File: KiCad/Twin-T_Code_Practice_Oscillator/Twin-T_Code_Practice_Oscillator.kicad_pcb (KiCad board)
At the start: 2 copper layers, 96.5 x 50.8 mm, 52 parts, among them J1 BATT, J2 DC IN, J3 PITCH, J4 VOLUME, J5 KEY, J6 PHONES, J7 SPKR, Q1 PN2222A, Q2 2N7000, U1 TLV272, U2 LM386

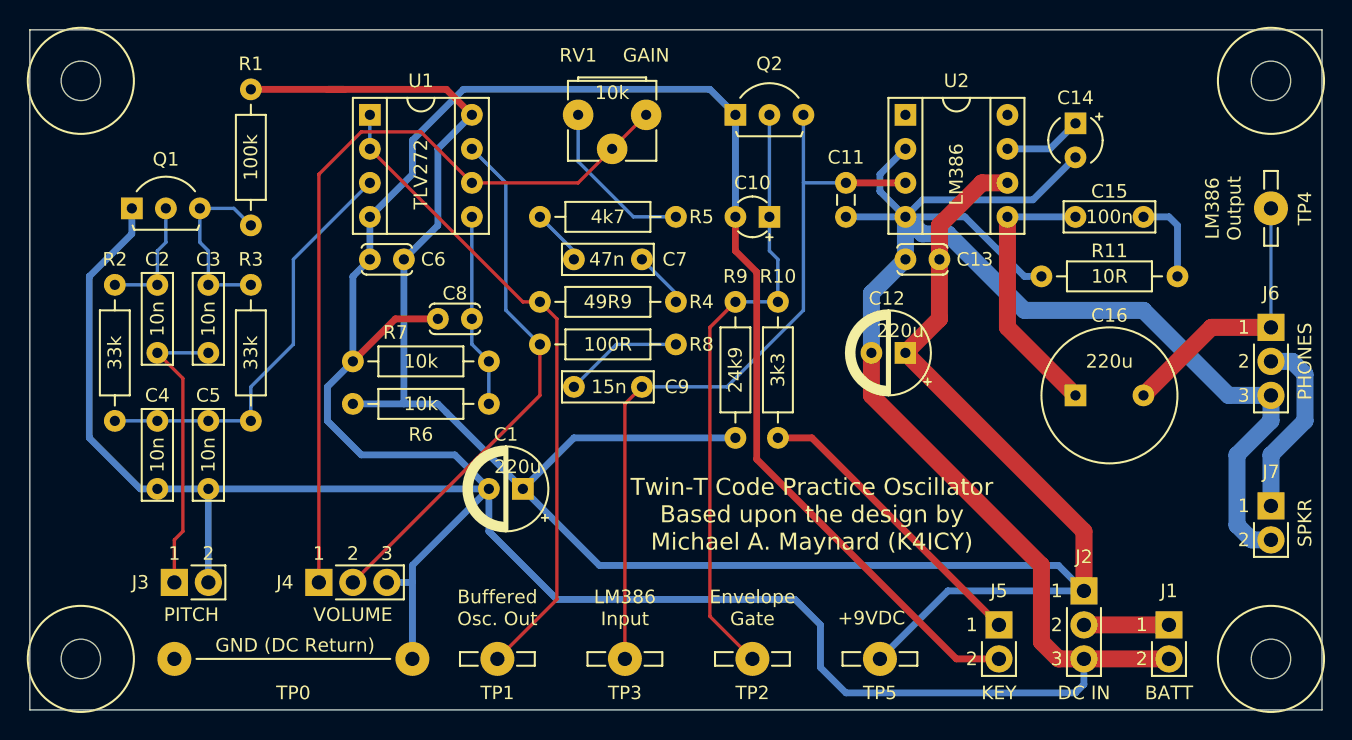
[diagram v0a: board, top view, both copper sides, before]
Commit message: Swapped LM386 inputs, tweaked PCB layout, updated BOM
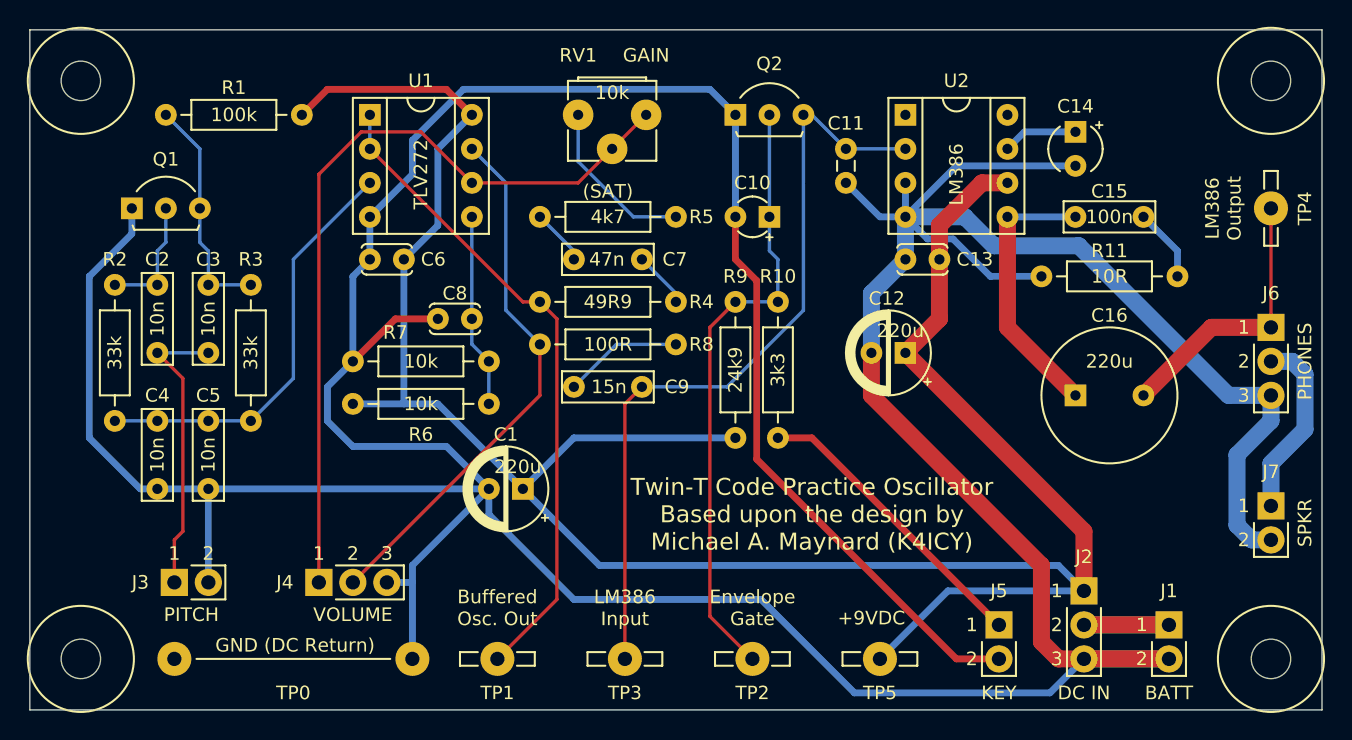
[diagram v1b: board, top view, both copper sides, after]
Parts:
- moved R1 10.4 mm to (111.8, 31.8), turned to 0 degrees
- moved C11 2.54 mm to (162.6, 36.8)
- moved C14 0.64 mm to (179.7, 33.0)
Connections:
- net Net-(C10-Pad1) renamed /Envelope_Gate
- net Net-(C16-Pad2) renamed /LM386_Out
- net Net-(C4-Pad2) renamed /Twin-T_Out
- net Net-(R4-Pad1) renamed /Buffered_Osc_Out
- C11 pad 2: Net-(C11-Pad2) -> /LM386_In
- C9 pad 1: Net-(C11-Pad2) -> /LM386_In
- Q2 pad 3: Net-(C11-Pad2) -> /LM386_In
- TP3 pad 1: Net-(C11-Pad2) -> /LM386_In
- U2 pad 2: GND -> /LM386_In
- U2 pad 3: Net-(C11-Pad2) -> GND
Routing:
- net /LM386_In: track 0.00 -> 58.5 mm
- net Net-(C11-Pad2): track 57.4 -> 0.00 mm
- net Net-(J1-Pad1): track 6.35 -> 12.7 mm
- net +9V: track 177.7 -> 173.4 mm
- net Net-(C3-Pad1): track 13.5 -> 17.2 mm
- net Net-(C15-Pad1): track 6.61 -> 5.50 mm
- net GND: track 386.0 -> 385.3 mm
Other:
- board text added: "(SAT)"
- board text added: "2020/09/01"
- board text removed: "2020/08/29"

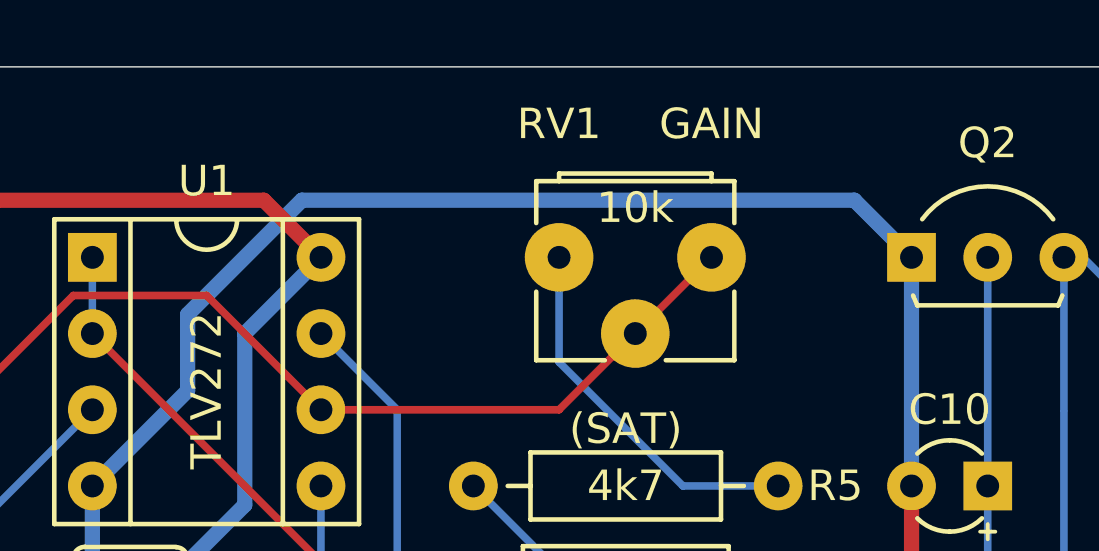
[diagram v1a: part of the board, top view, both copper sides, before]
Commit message: Replaced RV1. Cleaned up all docs
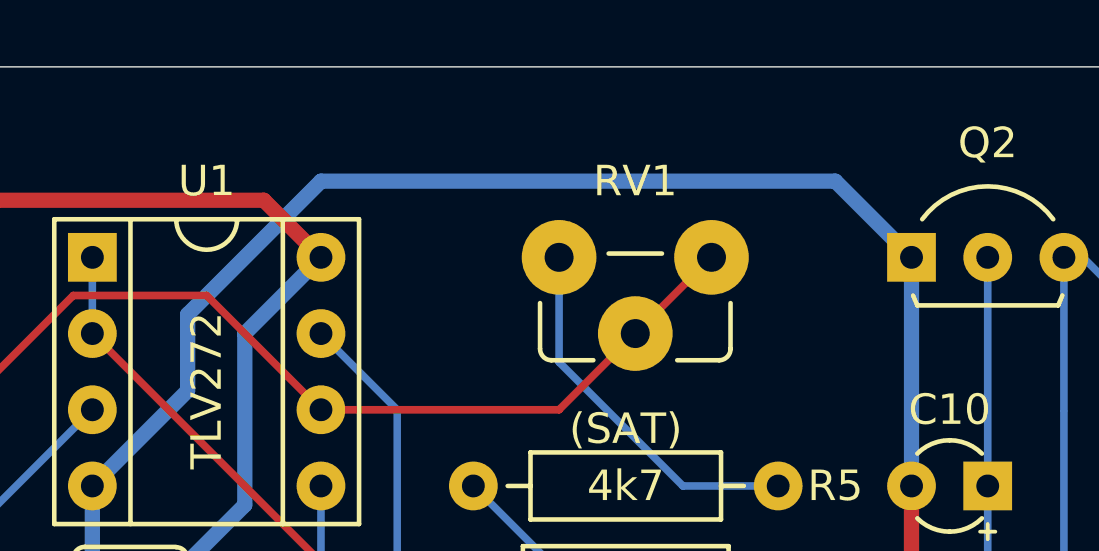
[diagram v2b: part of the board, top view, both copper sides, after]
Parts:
- RV1: footprint BE_TrimPot:Bourns_3329S_Vertical -> BE_TrimPot:Piher_PT6_Vertical
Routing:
- net GND: track 385.3 -> 385.9 mm
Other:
- board text added: "2020/09/02"
- board text removed: "2020/09/01"
